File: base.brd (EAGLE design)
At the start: 34 x 5.6 mm, 3 parts, among them J1 AS0A626-U2SN-7F, U2 XC7K160TFBG676

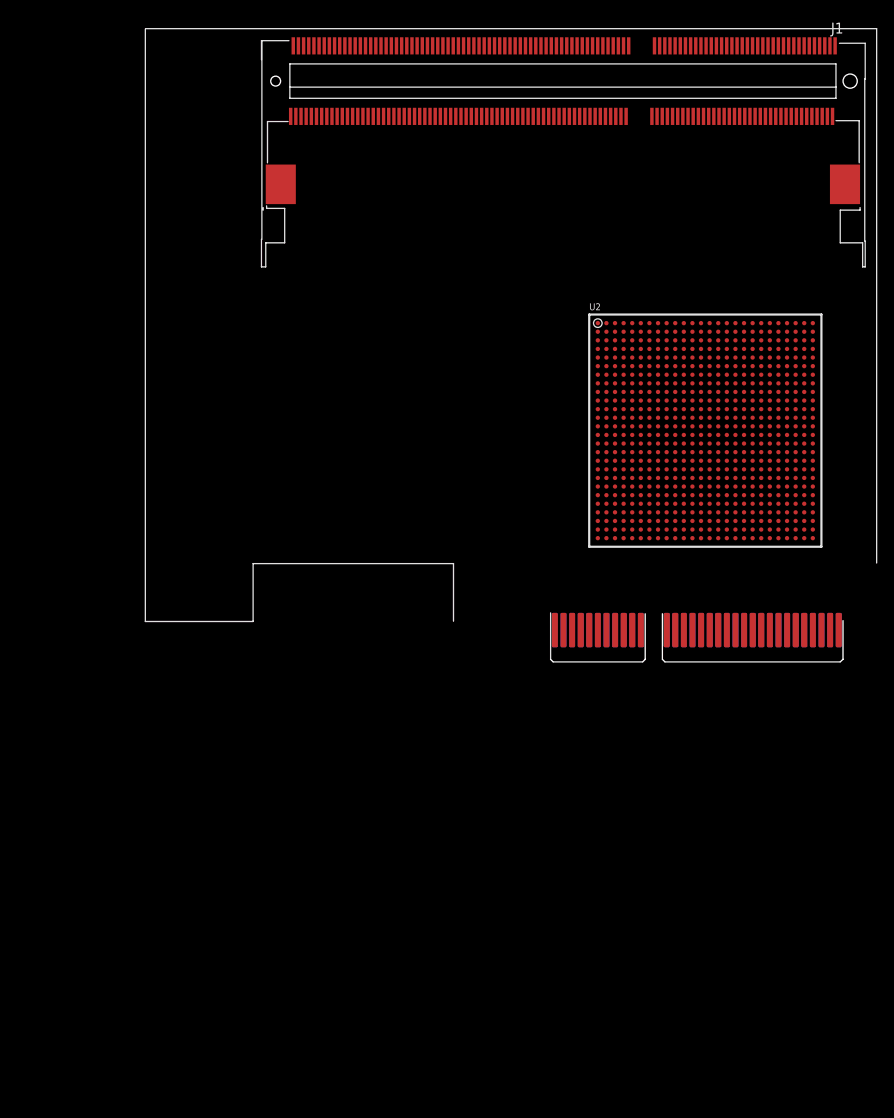
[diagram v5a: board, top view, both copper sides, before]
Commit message: updates, wired 33 + 34
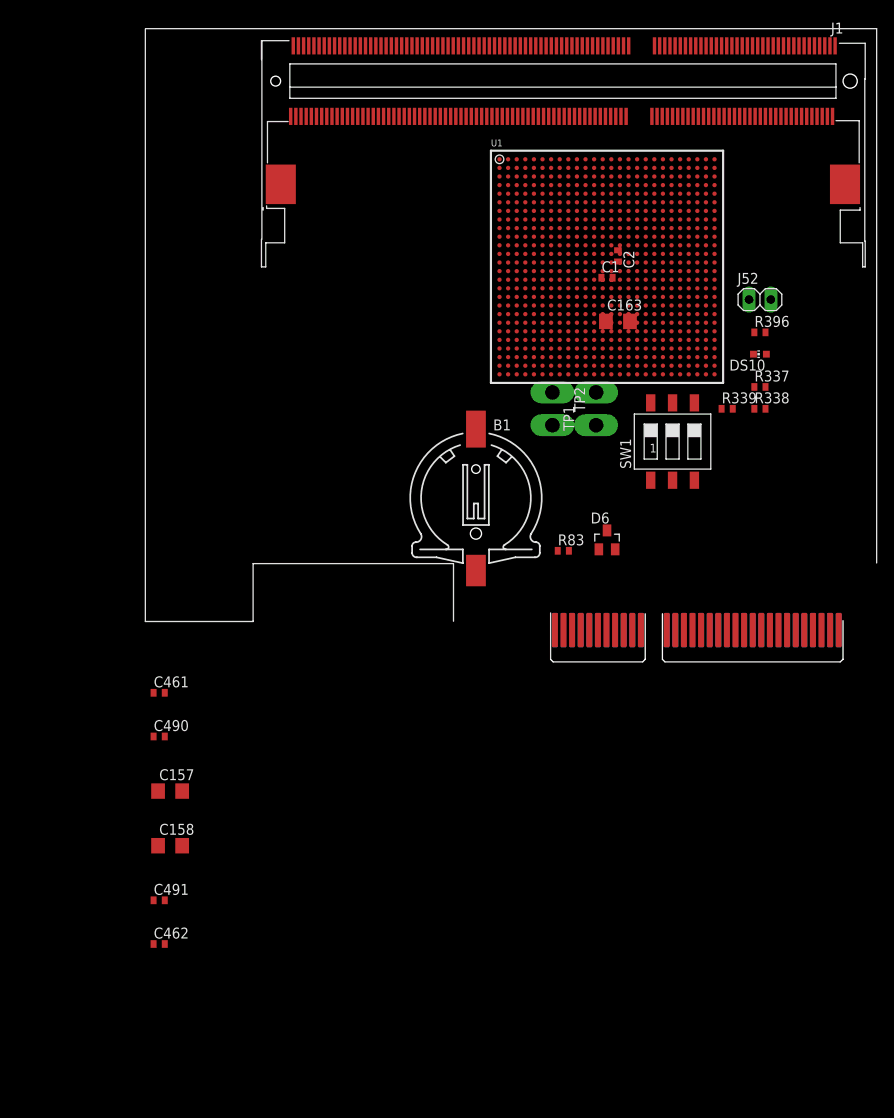
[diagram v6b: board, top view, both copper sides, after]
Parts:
- removed U2: XC7K160TFBG676, xilinx_devices_V6:FF676
- added B1: 1.5V seiko TS518FE_FL35E, battery:CH291-1220LF
- added C1, C2: .1uF, eagle-ltspice:C0402
- added C157, C158, C163: 100UF, eagle-ltspice:C1206
- added C461, C462, C490, C491: 0.1UF, eagle-ltspice:C0402
- added D6: BAS40-04, diode:SOT23
- added DS10: (no value), led:CHIP-LED0603
- added J52: (no value), pinhead:1X02
- added R337, R338, R339: 1.21K, eagle-ltspice:R0402
- added R396: 261, eagle-ltspice:R0402
- added R83: 4.7K, eagle-ltspice:R0402
- added SW1: (no value), smd-special:SMS-003
- added TP1, TP2: TP2P2-38-17, testpad:P2-38-17
- added U1: XC7A200TFBG676, xilinx_devices_V6_custom_labels:FF676
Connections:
- removed net D_A0: J1.98
- removed net D_A1: J1.97
- removed net D_A10: J1.107
- removed net D_A11: J1.84
- removed net D_A12: J1.83
- removed net D_A13: J1.119
- removed net D_A14: J1.80
- removed net D_A15: J1.78
- removed net D_A2: J1.96
- removed net D_A3: J1.95
- removed net D_A4: J1.92
- removed net D_A5: J1.91
- removed net D_A6: J1.90
- removed net D_A7: J1.86
- removed net D_A8: J1.89
- removed net D_A9: J1.85
- removed net D_BA0: J1.109
- removed net D_BA1: J1.108
- removed net D_BA2: J1.79
- removed net D_CAS_N: J1.115
- removed net D_CKE0: J1.73
- removed net D_CLK0_N: J1.103
- removed net D_CLK0_P: J1.101
- removed net D_CLK1_N: J1.104
- removed net D_CLK1_P: J1.102
- removed net D_D0: J1.5
- removed net D_D1: J1.7
- removed net D_D10: J1.33
- removed net D_D11: J1.35
- removed net D_D12: J1.22
- removed net D_D13: J1.24
- removed net D_D14: J1.34
- removed net D_D15: J1.36
- removed net D_D16: J1.39
- removed net D_D17: J1.41
- removed net D_D18: J1.51
- removed net D_D19: J1.53
- removed net D_D2: J1.15
- removed net D_D20: J1.40
- removed net D_D21: J1.42
- removed net D_D22: J1.50
- removed net D_D23: J1.52
- removed net D_D24: J1.57
- removed net D_D25: J1.59
- removed net D_D26: J1.67
- removed net D_D27: J1.69
- removed net D_D28: J1.56
- removed net D_D29: J1.58
- removed net D_D3: J1.17
- removed net D_D30: J1.68
- removed net D_D31: J1.70
- removed net D_D32: J1.129
- removed net D_D33: J1.131
- removed net D_D34: J1.141
- removed net D_D35: J1.143
- removed net D_D36: J1.130
- removed net D_D37: J1.132
- removed net D_D38: J1.140
- removed net D_D39: J1.142
- removed net D_D4: J1.4
- removed net D_D40: J1.147
- removed net D_D41: J1.149
- removed net D_D42: J1.157
- removed net D_D43: J1.159
- removed net D_D44: J1.146
- removed net D_D45: J1.148
- removed net D_D46: J1.158
- removed net D_D47: J1.160
- removed net D_D48: J1.163
- removed net D_D49: J1.165
- removed net D_D5: J1.6
- removed net D_D50: J1.175
- removed net D_D51: J1.177
- removed net D_D52: J1.164
- removed net D_D53: J1.166
- removed net D_D54: J1.174
- removed net D_D55: J1.176
- removed net D_D56: J1.181
- removed net D_D57: J1.183
- removed net D_D58: J1.191
- removed net D_D59: J1.193
- removed net D_D6: J1.16
- removed net D_D60: J1.180
- removed net D_D61: J1.182
- removed net D_D62: J1.192
- removed net D_D63: J1.194
- removed net D_D7: J1.18
- removed net D_D8: J1.21
- removed net D_D9: J1.23
- removed net D_DM0: J1.11
- removed net D_DM1: J1.28
- removed net D_DM2: J1.46
- removed net D_DM3: J1.63
- removed net D_DM4: J1.136
- removed net D_DM5: J1.153
- removed net D_DM6: J1.170
- removed net D_DM7: J1.187
- removed net D_DQS0_N: J1.10
- removed net D_DQS0_P: J1.12
- removed net D_DQS1_N: J1.27
- removed net D_DQS1_P: J1.29
- removed net D_DQS2_N: J1.45
- removed net D_DQS2_P: J1.47
- removed net D_DQS3_N: J1.62
- removed net D_DQS3_P: J1.64
- removed net D_DQS4_N: J1.135
- removed net D_DQS4_P: J1.137
- removed net D_DQS5_N: J1.152
- removed net D_DQS5_P: J1.154
- removed net D_DQS6_N: J1.169
- removed net D_DQS6_P: J1.171
- removed net D_DQS7_N: J1.186
- removed net D_DQS7_P: J1.188
- removed net D_NC: J1.120, J1.121, J1.122, J1.125, J1.74, J1.77
- removed net D_ODT0: J1.116
- removed net D_RAS_N: J1.110
- removed net D_RESET_N: J1.30
- removed net D_S0_N: J1.114
- removed net D_SCL: J1.202
- removed net D_SDA: J1.200
- removed net D_VSS: J1.127, J1.128, J1.13, J1.133, J1.134, J1.138, J1.139, J1.14, J1.144, J1.145, J1.150, J1.151, J1.155, J1.156, J1.161, J1.162, J1.167, J1.168, J1.172, J1.173, J1.178, J1.179, J1.184, J1.185, J1.189, J1.19, J1.190, J1.195, J1.196, J1.2, J1.20, J1.25, J1.26, J1.3, J1.31, J1.32, J1.37, J1.38, J1.43, J1.44, J1.48, J1.49, J1.54, J1.55, J1.60, J1.61, J1.65, J1.66, J1.71, J1.72, J1.8, J1.9
- removed net D_WE_N: J1.113
- removed net F_CCLK: U2.C8
- removed net F_DONE: U2.J7
- removed net F_INIT_N: U2.G7
- removed net F_M0: U2.T5
- removed net F_M1: U2.T2
- removed net F_M2: U2.P5
- removed net F_PROG_N: U2.P6
- removed net F_TCK_BUF: U2.L8
- removed net F_TDI_BUF: U2.R6
- removed net F_TDO: U2.R7
- removed net F_TMS_BUF: U2.N8
- removed net F_VBATT: U2.E8
- removed net VADJ_F: U2.A11, U2.AA21, U2.AC25, U2.AD22, U2.AF26, U2.B8, U2.C15, U2.D12, U2.E9, U2.G13, U2.H10, U2.K24, U2.N25, U2.P22, U2.R19, U2.T16, U2.T26, U2.U23, U2.V20, U2.Y24
- removed net VCC1V5_F: U2.AA1, U2.AA11, U2.AB18, U2.AB8, U2.AC15, U2.AC5, U2.AD12, U2.AD2, U2.AE19, U2.AE9, U2.AF16, U2.AF6, U2.U3, U2.V10, U2.W17, U2.W7, U2.Y14, U2.Y4
- removed net VCC1V5_FPGA: J1.100, J1.105, J1.106, J1.111, J1.112, J1.117, J1.118, J1.123, J1.75, J1.76, J1.81, J1.82, J1.87, J1.88, J1.93, J1.94, J1.99
- removed net VCC2V5_F: U2.A21, U2.B18, U2.C25, U2.D22, U2.E19, U2.F16, U2.F26, U2.G23, U2.H20, U2.J17, U2.L21, U2.L7, U2.M18, U2.P7, U2.T6
- removed net VTTDDR: J1.203, J1.204
- new net CPU_RESET: U1.U4
- new net DDR3_28: U1.W4
- new net DDR3_A0: U1.M4
- new net DDR3_A1: U1.J3
- new net DDR3_A10: U1.N7
- new net DDR3_A11: U1.L5
- new net DDR3_A12: U1.L7
- new net DDR3_A13: U1.N6
- new net DDR3_A14: U1.L3
- new net DDR3_A15: U1.K2
- new net DDR3_A2: U1.J1
- new net DDR3_A3: U1.L4
- new net DDR3_A4: U1.K5
- new net DDR3_A5: U1.M7
- new net DDR3_A6: U1.K1
- new net DDR3_A7: U1.M6
- new net DDR3_A8: U1.H1
- new net DDR3_A9: U1.K3
- new net DDR3_BA0: U1.N1
- new net DDR3_BA1: U1.M1
- new net DDR3_BA2: U1.H2
- new net DDR3_CAS_B: U1.T4
- new net DDR3_CKE0: U1.P4
- new net DDR3_CKE1: U1.N4
- new net DDR3_CLK0_N: U1.L2
- new net DDR3_CLK0_P: U1.M2
- new net DDR3_CLK1_N: U1.N2
- new net DDR3_CLK1_P: U1.N3
- new net DDR3_D0: U1.AB6
- new net DDR3_D1: U1.AA8
- new net DDR3_D10: U1.AF3
- new net DDR3_D11: U1.AE3
- new net DDR3_D12: U1.AD3
- new net DDR3_D13: U1.AC3
- new net DDR3_D14: U1.AB4
- new net DDR3_D15: U1.AA4
- new net DDR3_D16: U1.AC2
- new net DDR3_D17: U1.AB2
- new net DDR3_D18: U1.AF2
- new net DDR3_D19: U1.AE2
- new net DDR3_D2: U1.Y8
- new net DDR3_D20: U1.Y1
- new net DDR3_D21: U1.Y2
- new net DDR3_D22: U1.AC1
- new net DDR3_D23: U1.AB1
- new net DDR3_D24: U1.Y3
- new net DDR3_D25: U1.W3
- new net DDR3_D26: U1.W6
- new net DDR3_D27: U1.V6
- new net DDR3_D29: U1.W5
- new net DDR3_D3: U1.AB5
- new net DDR3_D30: U1.W1
- new net DDR3_D31: U1.V1
- new net DDR3_D4: U1.AA5
- new net DDR3_D5: U1.Y5
- new net DDR3_D6: U1.Y6
- new net DDR3_D7: U1.Y7
- new net DDR3_D8: U1.AF4
- new net DDR3_D9: U1.AF5
- new net DDR3_DM0: U1.AC6
- new net DDR3_DM1: U1.AC4
- new net DDR3_DM2: U1.AA3
- new net DDR3_DM3: U1.U7
- new net DDR3_DQS0_N: U1.W8
- new net DDR3_DQS0_P: U1.V8
- new net DDR3_DQS1_N: U1.AE5
- new net DDR3_DQS1_P: U1.AD5
- new net DDR3_DQS2_N: U1.AE1
- new net DDR3_DQS2_P: U1.AD1
- new net DDR3_DQS3_N: U1.V2
- new net DDR3_DQS3_P: U1.V3
- new net DDR3_ODT0: U1.R2
- new net DDR3_ODT1: U1.U2
- new net DDR3_RAS_B: U1.P1
- new net DDR3_RESET_B: U1.N8
- new net DDR3_S0_B: U1.T3
- new net DDR3_S1_B: U1.T2
- new net DDR3_TEMP_EVENT: U1.U1
- new net DDR3_WE_B: U1.R1
- new net FPGA_1V5: C157.1, C158.1, U1.AA1, U1.AC5, U1.AD2, U1.K4, U1.L1, U1.M8, U1.N5, U1.P2, U1.T6, U1.U3, U1.W7, U1.Y4
- new net FPGA_3V3: C163.1, SW1.4, SW1.5, SW1.6, U1.AB15, U1.W11, U1.Y14
- new net FPGA_CCLK: U1.H13
- new net FPGA_DONE: DS10.A, J52.1, R396.2, U1.W10
- new net FPGA_INIT_B: J52.2, U1.V11
- new net FPGA_M0: R337.2, SW1.3, U1.AB7
- new net FPGA_M1: R338.2, U1.Y9
- new net FPGA_M2: R339.2, SW1.1, U1.W9
- new net FPGA_PROG_B: U1.AE16
- new net FPGA_TCK_BUF: U1.H12
- new net FPGA_TDI_BUF: U1.H10
- new net FPGA_TMS_BUF: U1.H11
- new net FPGA_VBATT: B1.+, R83.1, U1.G14
- new net JTAG_TDO: U1.J10
- new net MGTAVCC: TP1.TP-1, U1.AA10, U1.AA12, U1.AC11, U1.AC13, U1.AC9, U1.D11, U1.D13, U1.D9, U1.F10, U1.F12
- new net MGTAVTT: TP2.TP-1, U1.AD15, U1.AD7, U1.AE10, U1.AE12, U1.AE14, U1.AE8, U1.B10, U1.B12, U1.B14, U1.B8, U1.C15, U1.C7
- new net N$10: U1.V4
- new net N$103: U1.P6
- new net N$105: U1.T5
- new net N$106: U1.R5
- new net N$107: U1.U6
- new net N$108: U1.U5
- new net N$109: U1.R8
- new net N$110: U1.P8
- new net N$111: U1.R7
- new net N$112: U1.R6
- new net N$113: U1.T8
- new net N$114: U1.T7
- new net N$116: U1.A1
- new net N$117: U1.C5
- new net N$118: U1.D2
- new net N$119: U1.F6
- new net N$120: U1.G3
- new net N$121: U1.J7
- new net N$122: U1.J8
- new net N$123: U1.E6
- new net N$124: U1.D6
- new net N$125: U1.H8
- new net N$126: U1.G8
- new net N$127: U1.H7
- new net N$128: U1.G7
- new net N$129: U1.F8
- new net N$130: U1.F7
- new net N$131: U1.H6
- new net N$132: U1.G6
- new net N$133: U1.H9
- new net N$134: U1.G9
- new net N$135: U1.J6
- new net N$136: U1.J5
- new net N$137: U1.L8
- new net N$138: U1.K8
- new net N$139: U1.J4
- new net N$140: U1.H4
- new net N$141: U1.K7
- new net N$142: U1.K6
- new net N$143: U1.G4
- new net N$144: U1.F4
- new net N$145: U1.G5
- new net N$146: U1.F5
- new net N$147: U1.E5
- new net N$148: U1.D5
- new net N$149: U1.D4
- new net N$150: U1.C4
- new net N$151: U1.B5
- new net N$152: U1.A5
- new net N$153: U1.B4
- new net N$154: U1.A4
- new net N$155: U1.D3
- new net N$156: U1.C3
- new net N$157: U1.F3
- new net N$158: U1.E3
- new net N$159: U1.C2
- new net N$160: U1.B2
- new net N$161: U1.A3
- new net N$162: U1.A2
- new net N$163: U1.C1
- new net N$164: U1.B1
- new net N$165: U1.F2
- new net N$166: U1.E2
- new net N$167: U1.E1
- new net N$168: U1.D1
- new net N$169: U1.G2
- new net N$170: U1.G1
- new net N$171: U1.H3
- new net N$34: U1.AA2
- new net N$4: U1.R12
- new net N$46: U1.AD4
- new net N$5: U1.R11
- new net N$59: U1.V9
- new net N$6: D6.1, R83.2
- new net SYSCLK_N: U1.P3
- new net SYSCLK_P: U1.R3
- new net VCC1V8: D6.2
- new net VCCAUX: U1.J9, U1.L9, U1.N9, U1.R9, U1.U9
- new net VCCBRAM: U1.N13, U1.R13, U1.U13, U1.W13
- new net VCCINT: U1.J11, U1.J13, U1.K10, U1.K12, U1.L11, U1.L13, U1.M10, U1.P10, U1.T10, U1.T12, U1.U11, U1.V10, U1.V12
- new net XADC_AGND: C1.2, C2.2, U1.M11, U1.N11
- new net XADC_VCC: C2.1, U1.M12
- new net XADC_VN_R_N: U1.P11
- new net XADC_VP_R_P: U1.N12
- new net XADC_VREFP: C1.1, U1.P12
- net GND: now also B1.-, C157.2, C158.2, C163.2, C461.2, C462.2, C490.2, C491.2, DS10.C, R337.1, R338.1, R339.1, TP1.TP-2, TP2.TP-2, U1.A10, U1.A12, U1.A14, U1.A16, U1.A26, U1.A6, U1.A8, U1.AA14, U1.AA16, U1.AA26, U1.AA6, U1.AA9, U1.AB10, U1.AB12, U1.AB14, U1.AB23, U1.AB3, U1.AB8, U1.AB9, U1.AC15, U1.AC20, U1.AC7, U1.AD11, U1.AD13, U1.AD16, U1.AD6, U1.AD9, U1.AE15, U1.AE24, U1.AE4, U1.AE6, U1.AF1, U1.AF10, U1.AF12, U1.AF14, U1.AF16, U1.AF21, U1.AF6, U1.AF8, U1.B15, U1.B16, U1.B23, U1.B3, U1.B6, U1.C11, U1.C13, U1.C16, U1.C20, U1.C6, U1.C9, U1.D15, U1.D17, U1.D7, U1.E10, U1.E12, U1.E14, U1.E15, U1.E24, U1.E4, U1.E7, U1.E8, U1.E9, U1.F1, U1.F14, U1.F21, U1.F9, U1.G10, U1.G11, U1.G12, U1.G13, U1.G18, U1.H25, U1.H5, U1.J12, U1.J2, U1.J22, U1.K11, U1.K13, U1.K19, U1.K9, U1.L10, U1.L12, U1.L16, U1.L26, U1.L6, U1.M13, U1.M23, U1.M3, U1.M9, U1.N10, U1.N20, U1.P13, U1.P17, U1.P7, U1.P9, U1.R10, U1.R24, U1.R4, U1.T1, U1.T11, U1.T13, U1.T21, U1.T9, U1.U10, U1.U12, U1.U18, U1.U8, U1.V13, U1.V15, U1.V25, U1.V5, U1.W12, U1.W2, U1.W22, U1.Y10, U1.Y11, U1.Y12, U1.Y13, U1.Y19; no longer J1.197, J1.198, J1.201, U2.A1, U2.A16, U2.A2, U2.A26, U2.A5, U2.A6, U2.A7, U2.AA16, U2.AA26, U2.AA6, U2.AB13, U2.AB23, U2.AB3, U2.AC10, U2.AC20, U2.AD17, U2.AD7, U2.AE14, U2.AE24, U2.AE4, U2.AF1, U2.AF11, U2.AF21, U2.B13, U2.B23, U2.B4, U2.B7, U2.C1, U2.C10, U2.C20, U2.C5, U2.C7, U2.D17, U2.D4, U2.D7, U2.E1, U2.E14, U2.E2, U2.E24, U2.E5, U2.E7, U2.F11, U2.F21, U2.F3, U2.F4, U2.F7, U2.G1, U2.G18, U2.G5, U2.G8, U2.H15, U2.H25, U2.H4, U2.H7, U2.J1, U2.J12, U2.J2, U2.J22, U2.J5, U2.K11, U2.K13, U2.K19, U2.K3, U2.K4, U2.K7, U2.K9, U2.L1, U2.L10, U2.L12, U2.L14, U2.L16, U2.L26, U2.L5, U2.M13, U2.M15, U2.M23, U2.M4, U2.M7, U2.M9, U2.N1, U2.N10, U2.N14, U2.N2, U2.N20, U2.N5, U2.N7, U2.P13, U2.P15, U2.P17, U2.P3, U2.P4, U2.P9, U2.R1, U2.R10, U2.R14, U2.R2, U2.R24, U2.R5, U2.R8, U2.T1, U2.T11, U2.T13, U2.T15, U2.T21, U2.T3, U2.T4, U2.T9, U2.U10, U2.U12, U2.U14, U2.U18, U2.U8, U2.V15, U2.V25, U2.V5, U2.W12, U2.W2, U2.W22, U2.Y19, U2.Y9
- net VCC3V3: now also R396.1; no longer J1.199
- net VTTVREF: now also C461.1, C462.1, C490.1, C491.1, U1.AA7, U1.M5, U1.P5, U1.V7; no longer J1.1, J1.124, J1.126

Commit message: adding 35
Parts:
- added C402: 100UF, eagle-ltspice:C1206
- added C463, C492: 0.1UF, eagle-ltspice:C0402
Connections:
- net N$123 renamed DDR3_D63
- net N$124 renamed DDR3_D62
- net N$125 renamed DDR3_D61
- net N$126 renamed DDR3_D60
- net N$127 renamed DDR3_DQS7_P
- net N$128 renamed DDR3_DQS7_N
- net N$129 renamed DDR3_D59
- net N$130 renamed DDR3_D58
- net N$131 renamed DDR3_D57
- net N$132 renamed DDR3_D56
- net N$133 renamed DDR3_DM7
- net N$135 renamed DDR3_D55
- net N$136 renamed DDR3_D54
- net N$137 renamed DDR3_D53
- net N$138 renamed DDR3_D52
- net N$139 renamed DDR3_DQS6_P
- net N$140 renamed DDR3_DQS6_N
- net N$141 renamed DDR3_D51
- net N$142 renamed DDR3_D50
- net N$143 renamed DDR3_D49
- net N$144 renamed DDR3_D48
- net N$145 renamed DDR3_DM6
- net N$147 renamed DDR3_D47
- net N$148 renamed DDR3_D46
- net N$149 renamed DDR3_D45
- net N$150 renamed DDR3_D44
- net N$151 renamed DDR3_DQS5_P
- net N$152 renamed DDR3_DQS5_N
- net N$153 renamed DDR3_D43
- net N$154 renamed DDR3_D42
- net N$155 renamed DDR3_D41
- net N$156 renamed DDR3_D40
- net N$157 renamed DDR3_DM5
- net N$159 renamed DDR3_D39
- net N$161 renamed DDR3_D38
- net N$162 renamed DDR3_D37
- net N$163 renamed DDR3_DQS4_P
- net N$164 renamed DDR3_DQS4_N
- net N$165 renamed DDR3_D36
- net N$166 renamed DDR3_D35
- net N$167 renamed DDR3_D34
- net N$168 renamed DDR3_D33
- net N$169 renamed DDR3_D32
- net N$170 renamed DDR3_DM4
- removed net N$119: U1.F6
- removed net N$134: U1.G9
- removed net N$160: U1.B2
- net FPGA_1V5: now also C402.1, U1.F6
- net GND: now also C402.2, C463.2, C492.2
- net VTTVREF: now also C463.1, C492.1, U1.B2, U1.G9
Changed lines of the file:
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@@
 <attribute name="SPICEPREFIX" value="C" x="16.51" y="-26.67" size="1.778" layer="27" display="off"/>
+</element>
+<element name="C402" library="eagle-ltspice" package="C1206" value="100UF" x="17.78" y="-33.02">
+<attribute name="SPICEMODEL" value="NONE" x="17.78" y="-33.02" size="1.778" layer="27" display="off"/>
+<attribute name="SPICEPREFIX" value="C" x="17.78" y="-33.02" size="1.778" layer="27" display="off"/>
+</element>
+<element name="C463" library="eagle-ltspice" package="C0402" value="0.1UF" x="16.51" y="-39.37">
+<attribute name="SPICEMODEL" value="NONE" x="16.51" y="-39.37" size="1.778" layer="27" display="off"/>
+<attribute name="SPICEPREFIX" value="C" x="16.51" y="-39.37" size="1.778" layer="27" display="off"/>
+</element>
+<element name="C492" library="eagle-ltspice" package="C0402" value="0.1UF" x="16.51" y="-44.45">
+<attribute name="SPICEMODEL" value="NONE" x="16.51" y="-44.45" size="1.778" layer="27" display="off"/>
+<attribute name="SPICEPREFIX" value="C" x="16.51" y="-44.45" size="1.778" layer="27" display="off"/>
 </element>
 </elements>
@@
 <contactref element="C462" pad="2"/>
 <contactref element="C491" pad="2"/>
+<contactref element="C402" pad="2"/>
+<contactref element="C463" pad="2"/>
+<contactref element="C492" pad="2"/>
 <wire x1="78.08" y1="63.57" x2="81.08" y2="64.57" width="0" layer="19" extent="1-1"/>
 <wire x1="79.08" y1="60.57" x2="78.08" y2="63.57" width="0" layer="19" extent="1-1"/>
@@
 <wire x1="17.16" y1="-21.59" x2="19.18" y2="-15.24" width="0" layer="19" extent="1-1"/>
 <wire x1="17.16" y1="-26.67" x2="17.16" y2="-21.59" width="0" layer="19" extent="1-1"/>
+<wire x1="19.18" y1="-33.02" x2="17.16" y2="-26.67" width="0" layer="19" extent="1-1"/>
+<wire x1="17.16" y1="-39.37" x2="19.18" y2="-33.02" width="0" layer="19" extent="1-1"/>
+<wire x1="17.16" y1="-44.45" x2="17.16" y2="-39.37" width="0" layer="19" extent="1-1"/>
 </signal>
 <signal name="N$6">
@@
 <contactref element="U1" pad="M8"/>
 <contactref element="C158" pad="1"/>
-<wire x1="60.08" y1="52.57" x2="63.08" y2="53.57" width="0" layer="19" extent="1-1"/>
-<wire x1="59.08" y1="55.57" x2="60.08" y2="52.57" width="0" layer="19" extent="1-1"/>
+<contactref element="C402" pad="1"/>
+<contactref element="U1" pad="F6"/>
+<wire x1="59.08" y1="55.57" x2="61.08" y2="59.57" width="0" layer="19" extent="1-1"/>
+<wire x1="60.08" y1="52.57" x2="59.08" y2="55.57" width="0" layer="19" extent="1-1"/>
+<wire x1="63.08" y1="53.57" x2="60.08" y2="52.57" width="0" layer="19" extent="1-1"/>
 <wire x1="56.08" y1="54.57" x2="59.08" y2="55.57" width="0" layer="19" extent="1-1"/>
 <wire x1="61.08" y1="49.57" x2="60.08" y2="52.57" width="0" layer="19" extent="1-1"/>
@@
 <wire x1="16.38" y1="-8.89" x2="57.08" y2="41.57" width="0" layer="19" extent="1-1"/>
 <wire x1="16.38" y1="-15.24" x2="16.38" y2="-8.89" width="0" layer="19" extent="1-1"/>
+<wire x1="16.38" y1="-33.02" x2="16.38" y2="-15.24" width="0" layer="19" extent="1-1"/>
 </signal>
 <signal name="N$10">
@@
 <contactref element="U1" pad="D2"/>
 </signal>
-<signal name="N$119">
-<contactref element="U1" pad="F6"/>
-</signal>
 <signal name="N$120">
 <contactref element="U1" pad="G3"/>
@@
 <contactref element="U1" pad="J8"/>
 </signal>
-<signal name="N$123">
+<signal name="DDR3_D63">
 <contactref element="U1" pad="E6"/>
 </signal>
-<signal name="N$124">
+<signal name="DDR3_D62">
 <contactref element="U1" pad="D6"/>
 </signal>
-<signal name="N$125">
+<signal name="DDR3_D61">
 <contactref element="U1" pad="H8"/>
 </signal>
-<signal name="N$126">
+<signal name="DDR3_D60">
 <contactref element="U1" pad="G8"/>
 </signal>
-<signal name="N$127">
+<signal name="DDR3_DQS7_P">
 <contactref element="U1" pad="H7"/>
 </signal>
-<signal name="N$128">
+<signal name="DDR3_DQS7_N">
 <contactref element="U1" pad="G7"/>
 </signal>
-<signal name="N$129">
+<signal name="DDR3_D59">
 <contactref element="U1" pad="F8"/>
 </signal>
-<signal name="N$130">
+<signal name="DDR3_D58">
 <contactref element="U1" pad="F7"/>
 </signal>
-<signal name="N$131">
+<signal name="DDR3_D57">
 <contactref element="U1" pad="H6"/>
 </signal>
-<signal name="N$132">
+<signal name="DDR3_D56">
 <contactref element="U1" pad="G6"/>
 </signal>
-<signal name="N$133">
+<signal name="DDR3_DM7">
 <contactref element="U1" pad="H9"/>
 </signal>
-<signal name="N$134">
-<contactref element="U1" pad="G9"/>
-</signal>
-<signal name="N$135">
+<signal name="DDR3_D55">
 <contactref element="U1" pad="J6"/>
 </signal>
-<signal name="N$136">
+<signal name="DDR3_D54">
 <contactref element="U1" pad="J5"/>
 </signal>
-<signal name="N$137">
+<signal name="DDR3_D53">
 <contactref element="U1" pad="L8"/>
 </signal>
-<signal name="N$138">
+<signal name="DDR3_D52">
 <contactref element="U1" pad="K8"/>
 </signal>
-<signal name="N$139">
+<signal name="DDR3_DQS6_P">
 <contactref element="U1" pad="J4"/>
 </signal>
-<signal name="N$140">
+<signal name="DDR3_DQS6_N">
 <contactref element="U1" pad="H4"/>
 </signal>
-<signal name="N$141">
+<signal name="DDR3_D51">
 <contactref element="U1" pad="K7"/>
 </signal>
-<signal name="N$142">
+<signal name="DDR3_D50">
 <contactref element="U1" pad="K6"/>
 </signal>
-<signal name="N$143">
+<signal name="DDR3_D49">
 <contactref element="U1" pad="G4"/>
 </signal>
-<signal name="N$144">
+<signal name="DDR3_D48">
 <contactref element="U1" pad="F4"/>
 </signal>
-<signal name="N$145">
+<signal name="DDR3_DM6">
 <contactref element="U1" pad="G5"/>
 </signal>
@@
 <contactref element="U1" pad="F5"/>
 </signal>
-<signal name="N$147">
+<signal name="DDR3_D47">
 <contactref element="U1" pad="E5"/>
 </signal>
-<signal name="N$148">
+<signal name="DDR3_D46">
 <contactref element="U1" pad="D5"/>
 </signal>
-<signal name="N$149">
+<signal name="DDR3_D45">
 <contactref element="U1" pad="D4"/>
 </signal>
-<signal name="N$150">
+<signal name="DDR3_D44">
 <contactref element="U1" pad="C4"/>
 </signal>
-<signal name="N$151">
+<signal name="DDR3_DQS5_P">
 <contactref element="U1" pad="B5"/>
 </signal>
-<signal name="N$152">
+<signal name="DDR3_DQS5_N">
 <contactref element="U1" pad="A5"/>
 </signal>
-<signal name="N$153">
+<signal name="DDR3_D43">
 <contactref element="U1" pad="B4"/>
 </signal>
-<signal name="N$154">
+<signal name="DDR3_D42">
 <contactref element="U1" pad="A4"/>
 </signal>
-<signal name="N$155">
+<signal name="DDR3_D41">
 <contactref element="U1" pad="D3"/>
 </signal>
-<signal name="N$156">
+<signal name="DDR3_D40">
 <contactref element="U1" pad="C3"/>
 </signal>
-<signal name="N$157">
+<signal name="DDR3_DM5">
 <contactref element="U1" pad="F3"/>
 </signal>
@@
 <contactref element="U1" pad="E3"/>
 </signal>
-<signal name="N$159">
+<signal name="DDR3_D39">
 <contactref element="U1" pad="C2"/>
 </signal>
-<signal name="N$160">
-<contactref element="U1" pad="B2"/>
-</signal>
-<signal name="N$161">
+<signal name="DDR3_D38">
 <contactref element="U1" pad="A3"/>
 </signal>
-<signal name="N$162">
+<signal name="DDR3_D37">
 <contactref element="U1" pad="A2"/>
 </signal>
-<signal name="N$163">
+<signal name="DDR3_DQS4_P">
 <contactref element="U1" pad="C1"/>
 </signal>
-<signal name="N$164">
+<signal name="DDR3_DQS4_N">
 <contactref element="U1" pad="B1"/>
 </signal>
-<signal name="N$165">
+<signal name="DDR3_D36">
 <contactref element="U1" pad="F2"/>
 </signal>
-<signal name="N$166">
+<signal name="DDR3_D35">
 <contactref element="U1" pad="E2"/>
 </signal>
-<signal name="N$167">
+<signal name="DDR3_D34">
 <contactref element="U1" pad="E1"/>
 </signal>
-<signal name="N$168">
+<signal name="DDR3_D33">
 <contactref element="U1" pad="D1"/>
 </signal>
-<signal name="N$169">
+<signal name="DDR3_D32">
 <contactref element="U1" pad="G2"/>
 </signal>
-<signal name="N$170">
+<signal name="DDR3_DM4">
 <contactref element="U1" pad="G1"/>
 </signal>
@@
 <contactref element="C491" pad="1"/>
 <contactref element="C462" pad="1"/>
+<contactref element="C492" pad="1"/>
+<contactref element="C463" pad="1"/>
+<contactref element="U1" pad="G9"/>
+<contactref element="U1" pad="B2"/>
+<wire x1="60.08" y1="53.57" x2="64.08" y2="58.57" width="0" layer="19" extent="1-1"/>
 <wire x1="60.08" y1="51.57" x2="60.08" y2="53.57" width="0" layer="19" extent="1-1"/>
 <wire x1="62.08" y1="47.57" x2="60.08" y2="51.57" width="0" layer="19" extent="1-1"/>
 <wire x1="62.08" y1="44.57" x2="62.08" y2="47.57" width="0" layer="19" extent="1-1"/>
+<wire x1="57.08" y1="63.57" x2="64.08" y2="58.57" width="0" layer="19" extent="1-1"/>
 <wire x1="15.86" y1="2.54" x2="62.08" y2="44.57" width="0" layer="19" extent="1-1"/>
 <wire x1="15.86" y1="-2.54" x2="15.86" y2="2.54" width="0" layer="19" extent="1-1"/>
 <wire x1="15.86" y1="-21.59" x2="15.86" y2="-2.54" width="0" layer="19" extent="1-1"/>
 <wire x1="15.86" y1="-26.67" x2="15.86" y2="-21.59" width="0" layer="19" extent="1-1"/>
+<wire x1="15.86" y1="-39.37" x2="15.86" y2="-26.67" width="0" layer="19" extent="1-1"/>
+<wire x1="15.86" y1="-44.45" x2="15.86" y2="-39.37" width="0" layer="19" extent="1-1"/>
 </signal>
 </signals>
